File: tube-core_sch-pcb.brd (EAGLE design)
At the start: 3.8 x 64 mm, 14 parts

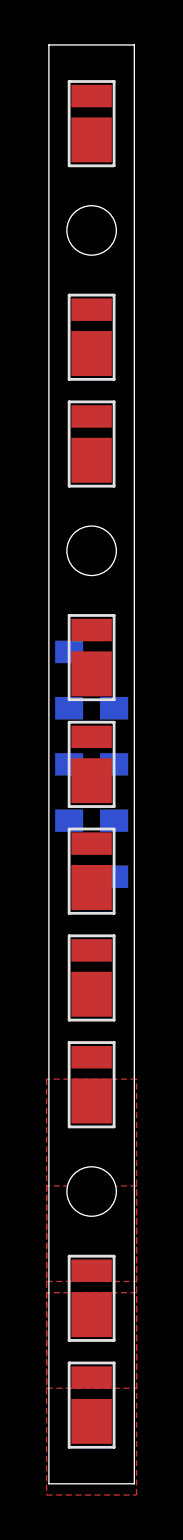
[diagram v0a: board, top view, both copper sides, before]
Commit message: Recreated core with new diodes
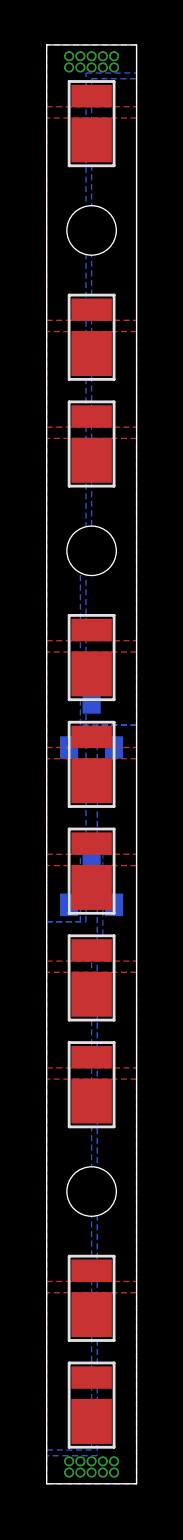
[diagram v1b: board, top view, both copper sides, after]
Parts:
- removed D10, D11, D12, D13: PMEG4010BEA, DIODES:SOD-323
- added D15, D16: BAV99, DIODES:SOT23-3
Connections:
- net ANODE: now also D15.3, D16.3; no longer D10.K, D11.K
- net CATHODE: now also D15.1, D16.1; no longer D12.A, D13.A
- net IN1: now also D15.2; no longer D11.A, D13.K
- net IN2: now also D16.2; no longer D10.A, D12.K
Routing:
- added copper zone on layer 1, net ANODE
- added copper zone on layer 16, net ANODE
- added copper zone on layer 1, net CATHODE
- added copper zone on layer 16, net CATHODE
- added copper zone on layer 16, net IN1
- added copper zone on layer 16, net IN2
- added copper zone on layer 1, net N$1
- added copper zone on layer 1, net N$19
- added copper zone on layer 1, net N$2
- added copper zone on layer 1, net N$3
- added copper zone on layer 1, net N$4
- added copper zone on layer 1, net N$5
- added copper zone on layer 1, net N$6
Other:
- board size 3.8 x 64 mm -> 4 x 64 mm

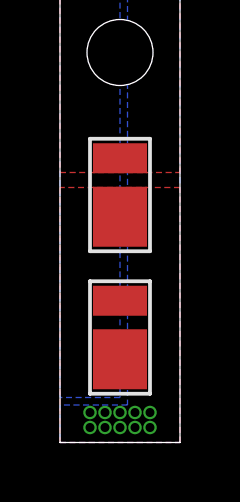
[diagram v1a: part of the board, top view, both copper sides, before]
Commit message: Tube core complete
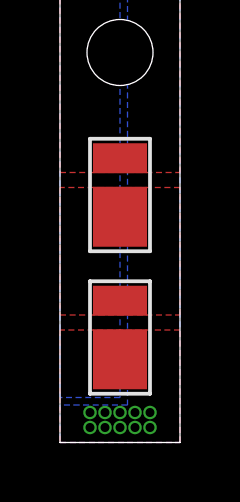
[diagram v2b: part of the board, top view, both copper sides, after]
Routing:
- added copper zone on layer 1, net N$7
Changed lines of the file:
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@@
 <?xml version="1.0" encoding="utf-8"?>
 <!DOCTYPE eagle SYSTEM "eagle.dtd">
-<eagle version="9.3.0">
+<eagle version="9.3.2">
 <drawing>
 <settings>
-<setting alwaysvectorfont="no"/>
+<setting alwaysvectorfont="yes"/>
 <setting verticaltext="up"/>
 </settings>
@@
 </layers>
 <board>
-<fusionsync huburn="a.cGVyc29uYWw6dWUyYjllNWFm" projecturn="a.cGVyc29uYWw6dWUyYjllNWFmIzIwMTkxMDE5MjI4NzM0NTgx" f3durn="urn:adsk.wipprod:dm.lineage:c_JeT0lITXCc1k8J0YYWbw" pcbguid="5d53bc27-9163-4ab3-a22c-c60f97ca62a7" lastpulledtime="2019-10-21T11:33:37Z" lastsyncedchangeguid="4d73dcee-b243-351e-f895-339cf1dc7faa"/>
+<fusionsync huburn="a.cGVyc29uYWw6dWUyYjllNWFm" projecturn="a.cGVyc29uYWw6dWUyYjllNWFmIzIwMTkxMDE5MjI4NzM0NTgx" f3durn="urn:adsk.wipprod:dm.lineage:c_JeT0lITXCc1k8J0YYWbw" pcbguid="5d53bc27-9163-4ab3-a22c-c60f97ca62a7" lastpulledtime="2019-10-21T11:33:37Z" lastsyncedchangeguid="ada0fcd0-7678-9317-fd19-94206f447312"/>
 <plain>
 <hole x="0" y="9.5" drill="2.2"/>
@@
 </element>
 <element name="D15" library="DIODES" package="SOT23-3" value="BAV99" x="0" y="1.75" smashed="yes" rot="MR0">
+<attribute name="DIGIKEY" value="BAV99Q-7-FDICT-ND" x="0" y="1.75" size="1.778" layer="28" rot="MR0" display="off"/>
+<attribute name="HEIGHT" value="1.2" x="0" y="1.75" size="1.778" layer="28" rot="MR0" display="off"/>
 <attribute name="NAME" x="1.75" y="3.625" size="1" layer="26" rot="MR0"/>
+<attribute name="PRICE_PER" value="0.15" x="0" y="1.75" size="1.778" layer="28" rot="MR0" display="off"/>
+<attribute name="VALUE" value="BAV99" x="0" y="1.75" size="1.778" layer="28" rot="MR0" display="off"/>
 </element>
 <element name="D16" library="DIODES" package="SOT23-3" value="BAV99" x="0" y="-5.25" smashed="yes" rot="MR0">
+<attribute name="DIGIKEY" value="BAV99Q-7-FDICT-ND" x="0" y="-5.25" size="1.778" layer="28" rot="MR0" display="off"/>
+<attribute name="HEIGHT" value="1.2" x="0" y="-5.25" size="1.778" layer="28" rot="MR0" display="off"/>
 <attribute name="NAME" x="-1.75" y="-7.125" size="1" layer="26" rot="MR180"/>
+<attribute name="PRICE_PER" value="0.15" x="0" y="-5.25" size="1.778" layer="28" rot="MR0" display="off"/>
+<attribute name="VALUE" value="BAV99" x="0" y="-5.25" size="1.778" layer="28" rot="MR0" display="off"/>
 </element>
 </elements>
@@
 <polygon width="0.15" layer="1">
 <vertex x="2" y="-32"/>
-<vertex x="2" y="-23.5"/>
-<vertex x="-2" y="-23.5"/>
+<vertex x="2" y="-28.25"/>
+<vertex x="-2" y="-28.25"/>
 <vertex x="-2" y="-32"/>
 </polygon>
@@
 <contactref element="D9" pad="K"/>
 <contactref element="D14" pad="A"/>
-<wire x1="0" y1="-24.475" x2="0" y2="-27.275" width="0" layer="19" extent="1-1"/>
+<polygon width="0.15" layer="1">
+<vertex x="2" y="-27.75"/>
+<vertex x="2" y="-23.5"/>
+<vertex x="-2" y="-23.5"/>
+<vertex x="-2" y="-27.75"/>
+</polygon>
 </signal>
 <signal name="IN1">

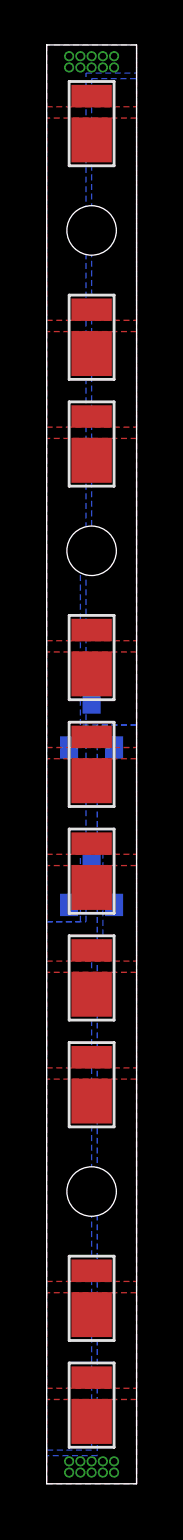
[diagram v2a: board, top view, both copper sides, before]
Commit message: New LED design
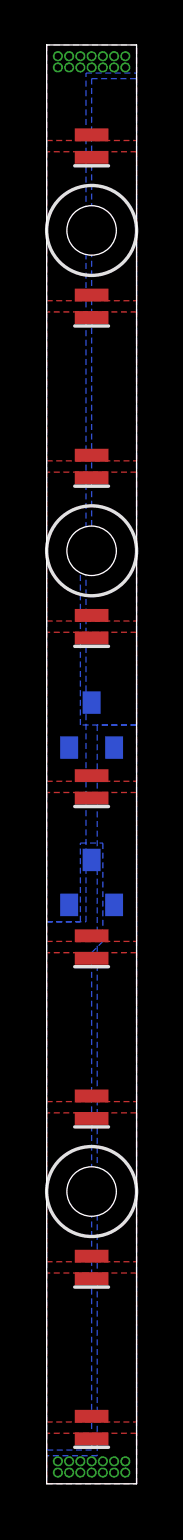
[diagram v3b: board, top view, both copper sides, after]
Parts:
- removed D14: 3500K, OPTO:JE2835AWT
- D1, D2, D3, D4, D5, D6, D7, D8, D9: value 3500K -> 3000K; device OPTO:JE2835AWT -> OPTO:MP-1616
- moved D8 8.12 mm to (0.00, -22.4), turned to 270 degrees
- moved D7 5.75 mm to (0.00, -15.2), turned to 270 degrees
- moved D9 5.75 mm to (0.00, -29.5), turned to 270 degrees
- moved D6 3.38 mm to (0.00, -8.12), turned to 270 degrees
- moved D2 1.38 mm to (0.00, 20.4), turned to 270 degrees
- moved D4 1.38 mm to (0.00, 6.12), turned to 270 degrees
- moved D1 1.00 mm to (0.00, 27.5), turned to 270 degrees
- moved D3 1.00 mm to (0.00, 13.2), turned to 270 degrees
- moved D5 1.00 mm to (0.00, -1.00), turned to 270 degrees
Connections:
- removed net N$7 (its old number): D14.A, D9.K
- net CATHODE: now also D9.K; no longer D14.K
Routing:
- removed copper zone on layer 1, net N$7 (its old number)
